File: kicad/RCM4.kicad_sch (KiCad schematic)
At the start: 17 parts, among them U1 74LVC1G07SE-7

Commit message: J4 outer row to GND, route SPI0 CE0/CE1, PCB review fixes
Schematic: J4 pins 6, 8, 10, 16, 18 (GPIO21, GPIO20, GPIO1, GPIO23,
GPIO18) are now GND; CM4 pins 25, 27, 35, 47, 49 get no-connect flags.
The five labels, wires and CM4_Connectors sheet pins are removed.

PCB: J4 pad nets updated to match, SPI0_CE0 and SPI0_CE1 routed to the
CM4, the 11 inner J4 nets restored.

Review fixes:
- PGND: solid zone connections on In1 for J1 pin 2 and the RoboClaw
  BAT- pins (were thermal spokes carrying the motor return).
- FUSE_IN: zone outlines widened below the fuse pads so the Q1 source
  arm is ~4 mm instead of 1.2 mm; two more 1.0 mm vias.
- HD2 pair rerouted as a coupled pair on B.Cu through the USB-A pin
  corridor; HD2_P via moved.
- Second 5V via at the U4 input.
- Pair length matching: meanders on EP0-, EP1-, EP2+, EP3-, USB_HUB_N,
  HSD2-, HD1_N; RJ45 legs end at the pin centres. All pairs within
  0.03 mm.
- RF_IN from CN1 re-routed at the 0.18 mm class width (was 1.0/0.3 mm).

Project: DRC exclusions for the silk-to-edge warnings.
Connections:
- net GPIO1: no longer names the net of Module1.35 (ID_SC)
- net GPIO18: no longer names the net of Module1.49 (GPIO18)
- net GPIO20: no longer names the net of Module1.27 (GPIO20)
- net GPIO21: no longer names the net of Module1.25 (GPIO21)
- net GPIO23: no longer names the net of Module1.47 (GPIO23)
- no-connect marks 92 -> 97
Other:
- sheet CM4_Connectors ports: added none; removed GPIO1, GPIO18, GPIO20, GPIO21, GPIO23
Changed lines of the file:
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@@
 	)
 	(no_connect
+		(at 111.76 58.42)
+	)
+	(no_connect
+		(at 111.76 60.96)
+	)
+	(no_connect
+		(at 111.76 71.12)
+	)
+	(no_connect
+		(at 111.76 86.36)
+	)
+	(no_connect
+		(at 111.76 88.9)
+	)
+	(no_connect
 		(at 111.76 104.14)
 	)
@@
 	(wire
 		(pts
-			(xy 111.76 71.12) (xy 116.84 71.12)
-		)
-		(stroke
-			(width 0)
-			(type default)
-		)
-	)
-	(wire
-		(pts
 			(xy 26.67 147.32) (xy 31.75 147.32)
 		)
@@
 	(wire
 		(pts
-			(xy 252.73 152.4) (xy 247.65 152.4)
-		)
-		(stroke
-			(width 0)
-			(type default)
-		)
-	)
-	(wire
-		(pts
 			(xy 220.98 119.38) (xy 220.98 127)
 		)
@@
 	(wire
 		(pts
-			(xy 111.76 86.36) (xy 116.84 86.36)
-		)
-		(stroke
-			(width 0)
-			(type default)
-		)
-	)
-	(wire
-		(pts
 			(xy 128.27 184.15) (xy 128.27 182.88)
 		)
@@
 	(wire
 		(pts
-			(xy 111.76 88.9) (xy 116.84 88.9)
-		)
-		(stroke
-			(width 0)
-			(type default)
-		)
-	)
-	(wire
-		(pts
 			(xy 154.94 104.14) (xy 154.94 96.52)
 		)
@@
 	(wire
 		(pts
-			(xy 252.73 137.16) (xy 247.65 137.16)
-		)
-		(stroke
-			(width 0)
-			(type default)
-		)
-	)
-	(wire
-		(pts
-			(xy 111.76 60.96) (xy 116.84 60.96)
-		)
-		(stroke
-			(width 0)
-			(type default)
-		)
-	)
-	(wire
-		(pts
 			(xy 48.26 119.38) (xy 50.8 119.38)
 		)
@@
 	(wire
 		(pts
-			(xy 252.73 116.84) (xy 247.65 116.84)
-		)
-		(stroke
-			(width 0)
-			(type default)
-		)
-	)
-	(wire
-		(pts
 			(xy 154.94 187.96) (xy 157.48 187.96)
 		)
@@
 	(wire
 		(pts
-			(xy 252.73 142.24) (xy 247.65 142.24)
-		)
-		(stroke
-			(width 0)
-			(type default)
-		)
-	)
-	(wire
-		(pts
 			(xy 35.56 185.42) (xy 33.02 185.42)
 		)
@@
 	(wire
 		(pts
-			(xy 111.76 58.42) (xy 116.84 58.42)
-		)
-		(stroke
-			(width 0)
-			(type default)
-		)
-	)
-	(wire
-		(pts
 			(xy 252.73 127) (xy 247.65 127)
 		)
@@
 	(wire
 		(pts
-			(xy 252.73 139.7) (xy 247.65 139.7)
-		)
-		(stroke
-			(width 0)
-			(type default)
-		)
-	)
-	(wire
-		(pts
 			(xy 48.26 91.44) (xy 50.8 91.44)
 		)
@@
 		)
 	)
-	(label "GPIO20"
-		(at 247.65 137.16 180)
-		(effects
-			(font
-				(size 1.27 1.27)
-			)
-			(justify right)
-		)
-	)
 	(label "PGOOD_12V"
 		(at 250.19 161.29 180)
@@
 		)
 	)
-	(label "GPIO1"
-		(at 116.84 71.12 0)
-		(effects
-			(font
-				(size 1.27 1.27)
-			)
-			(justify left)
-		)
-	)
 	(label "EP2-"
 		(at 118.11 38.1 0)
@@
 		)
 	)
-	(label "GPIO1"
-		(at 247.65 152.4 180)
-		(effects
-			(font
-				(size 1.27 1.27)
-			)
-			(justify right)
-		)
-	)
 	(label "~{FLT}"
 		(at 250.19 163.83 180)
@@
 		)
 	)
-	(label "GPIO18"
-		(at 116.84 88.9 0)
-		(effects
-			(font
-				(size 1.27 1.27)
-			)
-			(justify left)
-		)
-	)
 	(label "I2C1_SDA"
 		(at 45.72 99.06 180)
@@
 		)
 	)
-	(label "GPIO21"
-		(at 247.65 139.7 180)
-		(effects
-			(font
-				(size 1.27 1.27)
-			)
-			(justify right)
-		)
-	)
 	(label "BOOT_CONSOLE_TXD"
 		(at 116.84 96.52 0)
@@
 		)
 	)
-	(label "GPIO21"
-		(at 116.84 58.42 0)
-		(effects
-			(font
-				(size 1.27 1.27)
-			)
-			(justify left)
-		)
-	)
 	(label "SPI0_MOSI"
 		(at 247.65 127 180)
@@
 		)
 	)
-	(label "GPIO23"
-		(at 116.84 86.36 0)
-		(effects
-			(font
-				(size 1.27 1.27)
-			)
-			(justify left)
-		)
-	)
-	(label "GPIO23"
-		(at 247.65 142.24 180)
-		(effects
-			(font
-				(size 1.27 1.27)
-			)
-			(justify right)
-		)
-	)
 	(label "3V3_CM4"
 		(at 247.65 38.1 180)
@@
 		)
 	)
-	(label "GPIO20"
-		(at 116.84 60.96 0)
-		(effects
-			(font
-				(size 1.27 1.27)
-			)
-			(justify left)
-		)
-	)
 	(label "SPI0_MOSI"
 		(at 45.72 81.28 180)
@@
 		)
 	)
-	(label "GPIO18"
-		(at 247.65 116.84 180)
-		(effects
-			(font
-				(size 1.27 1.27)
-			)
-			(justify right)
-		)
-	)
 	(label "3V3_CM4"
 		(at 44.45 124.46 180)
@@
 		)
 	)
-	(sheet
+(sheet
 		(at 252.73 81.28)
 		(size 25.4 73.66)
@@
 			)
 		)
-		(pin "GPIO18" bidirectional
-			(at 252.73 116.84 180)
-			(effects
-				(font
-					(size 1.27 1.27)
-				)
-				(justify left)
-			)
-		)
 		(pin "GPIO19" bidirectional
 			(at 252.73 134.62 180)
@@
 			)
 		)
-		(pin "GPIO20" bidirectional
-			(at 252.73 137.16 180)
-			(effects
-				(font
-					(size 1.27 1.27)
-				)
-				(justify left)
-			)
-		)
-		(pin "GPIO21" bidirectional
-			(at 252.73 139.7 180)
-			(effects
-				(font
-					(size 1.27 1.27)
-				)
-				(justify left)
-			)
-		)
-		(pin "GPIO23" bidirectional
-			(at 252.73 142.24 180)
-			(effects
-				(font
-					(size 1.27 1.27)
-				)
-				(justify left)
-			)
-		)
 		(pin "GPIO26" bidirectional
 			(at 252.73 144.78 180)
@@
 			(effects
 				(font
-					(size 1.27 1.27)
-				)
-				(justify left)
-			)
-		)
-		(pin "GPIO1" bidirectional
-			(at 252.73 152.4 180)
-			(effects
-				(font

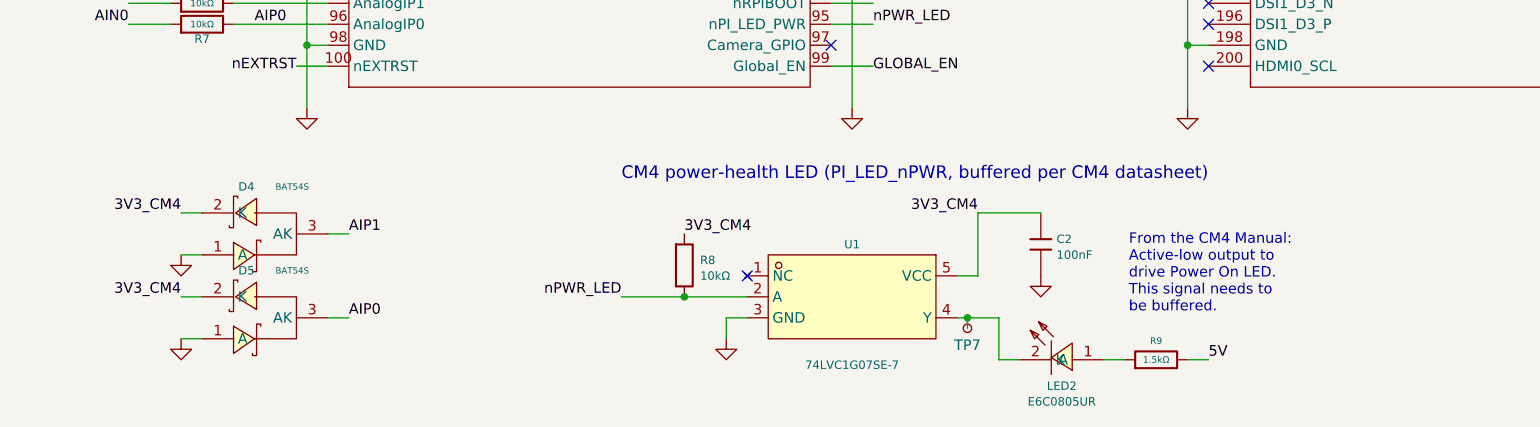
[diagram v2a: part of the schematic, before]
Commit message: Added I2C and battery 3d file
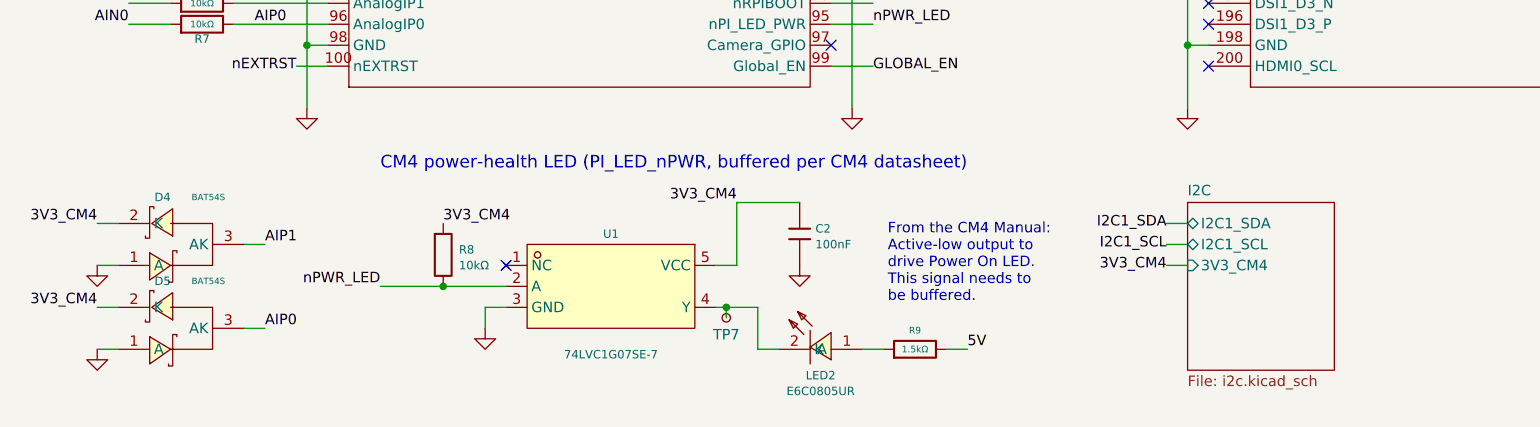
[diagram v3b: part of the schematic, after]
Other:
- added sheet I2C (i2c.kicad_sch)
- moved on the sheet: C2, D4, D5, LED2, R8, R9, TP7, U1
